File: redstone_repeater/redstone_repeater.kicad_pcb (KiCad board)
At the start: 2 copper layers, 40 x 40 mm, 46 parts, among them J1 1x4_Pogo, J2 1x4_Pogo, J3 1x4_Pogo, J4 1x4_Pogo, J5 1x4_Pogo, J6 1x4_Pogo, J7 1x4_Pogo, J8 1x4_Pogo, J9 2.54mm_ProgrammingPin, Q1 BC108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

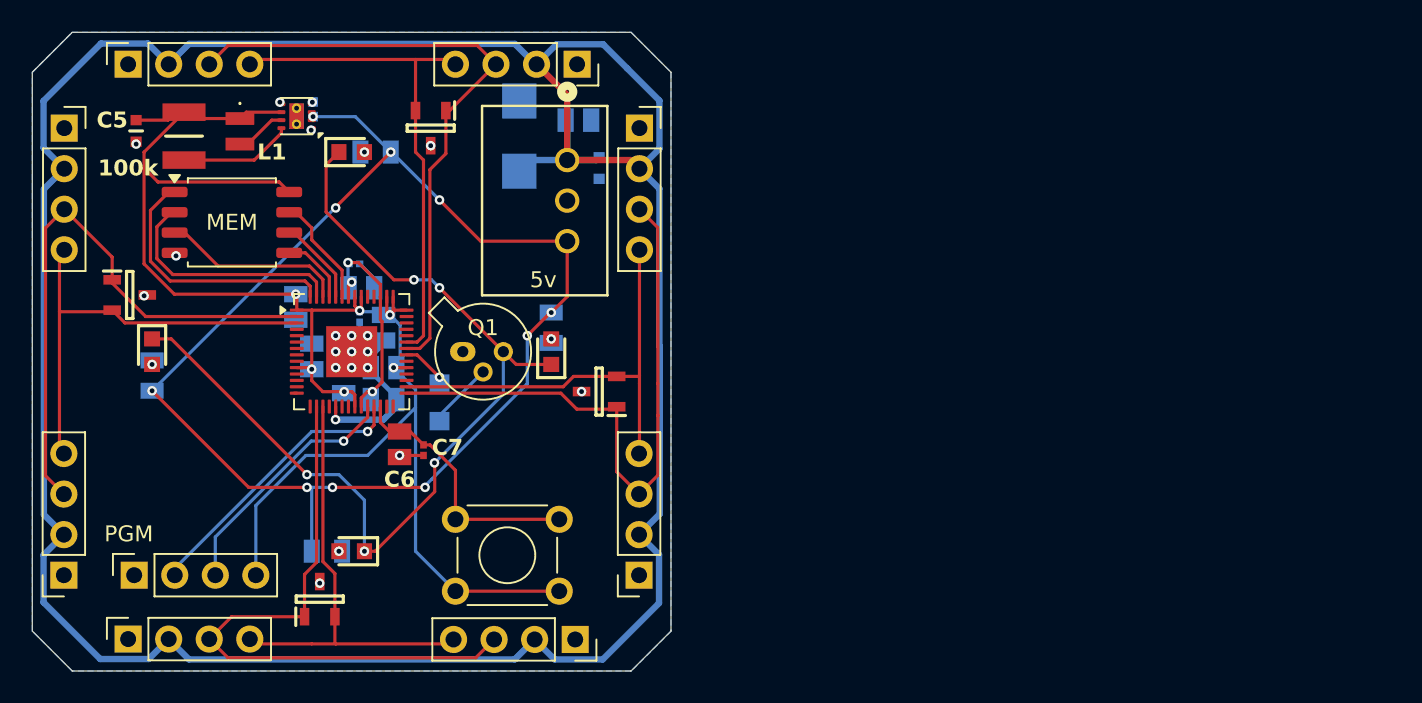
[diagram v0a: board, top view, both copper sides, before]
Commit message: add four individually controlled leds for repeater, small adjustments for redstone dust
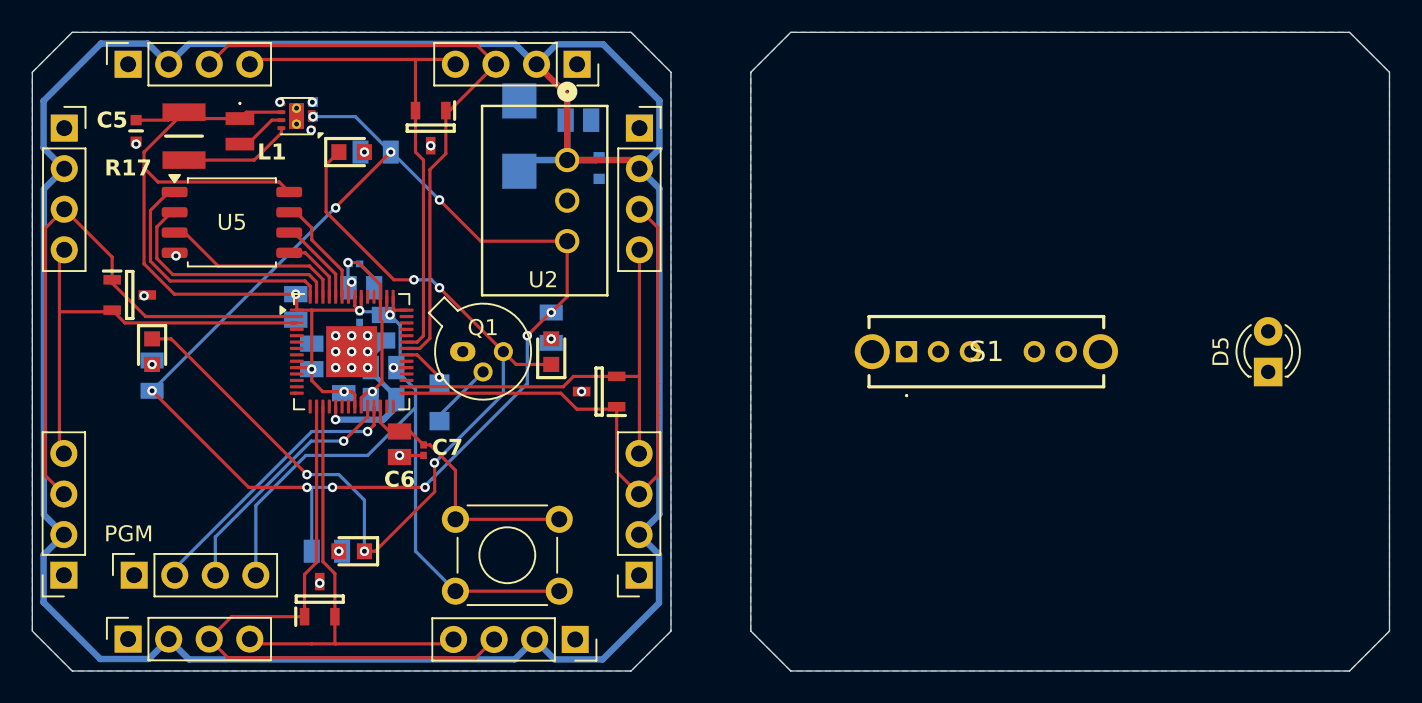
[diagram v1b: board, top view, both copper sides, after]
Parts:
- added D5: LED, LED_THT:LED_D3.0mm, F.Cu at (192.4, 56.3)
- added S1: SLW-1478144-5A-S-D, SamacSys_Parts:SLW14781445ASD, F.Cu at (169.8, 55.0)
- renumbered 200 to R1, 100k to R17, 1k to R5, 5v to U2, MEM to U5
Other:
- board size 40 x 40 mm -> 85 x 40 mm

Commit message: reorganize pcb layout for redstone repeater
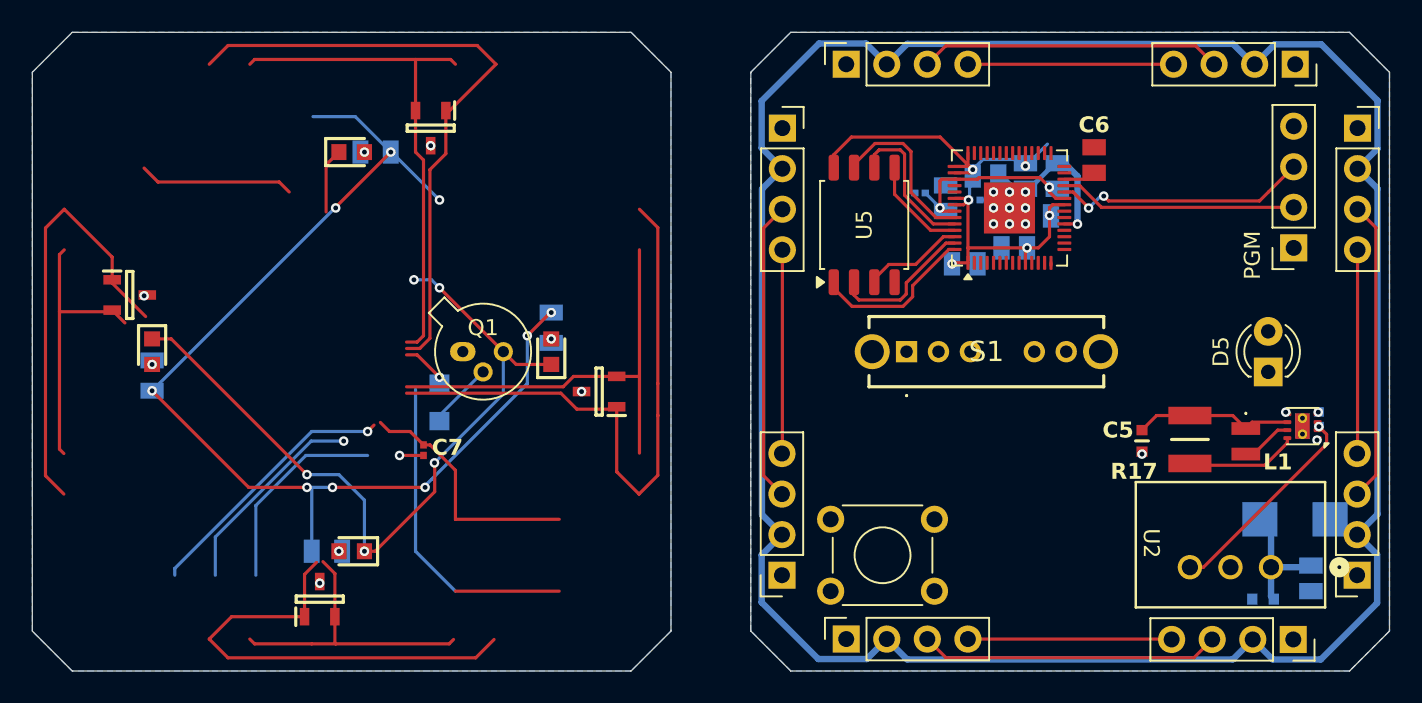
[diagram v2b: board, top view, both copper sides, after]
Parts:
- moved J9 75.5 mm to (194.0, 48.5), turned to 180 degrees
- moved C1 65.9 mm to (195.6, 59.2)
- moved C5 65.9 mm to (184.5, 60.6)
- moved L1 65.9 mm to (191.0, 60.6)
- moved U3 65.9 mm to (194.6, 59.7)
- moved R17 65.8 mm to (187.5, 60.5)
- moved D19 54.2 mm to (194.1, 65.5), turned to 0 degrees
- moved C3 54.1 mm to (195.1, 69.2), turned to -90 degrees
- moved U2 50.9 mm to (192.6, 68.5), turned to 180 degrees
- moved C4 49.6 mm to (192.1, 70.5), turned to 180 degrees
- moved C6 47.0 mm to (181.5, 43.0), turned to 90 degrees
- moved J1 45.0 mm to (166.0, 37.0)
- moved J2 45.0 mm to (194.1, 37.0)
- moved J3 45.0 mm to (198.0, 41.0)
- moved J4 45.0 mm to (198.0, 69.0)
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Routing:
- net /N_TX: track 39.7 -> 58.6 mm
- net /E_TX: track 38.5 -> 57.3 mm
- net /3.3V_LOCAL: track 105.0 -> 90.7 mm
- net Net-(J9-Pin_2): track 17.8 -> 31.5 mm
- net Net-(J9-Pin_3): track 15.7 -> 29.0 mm, vias 1 -> 3
- net /N_RX: track 31.9 -> 44.7 mm
- net /E_RX: track 27.6 -> 40.4 mm
- net VCC: track 173.7 -> 162.1 mm
- net /W_TX: track 37.1 -> 46.4 mm
- net /S_TX: track 38.8 -> 47.9 mm
- net Net-(D1-K): track 59.7 -> 52.5 mm
- net Net-(U1-QSPI_SS): track 17.0 -> 10.3 mm
- net Net-(U1-QSPI_SD1): track 15.0 -> 9.12 mm
- net Net-(U1-QSPI_SD2): track 12.2 -> 6.33 mm
- net Net-(U1-QSPI_SCLK): track 5.37 -> 9.39 mm
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
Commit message: finalize schematic and finish layout of pcb
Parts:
- added Q2: MMBT3904, Package_TO_SOT_SMD:SOT-23, F.Cu at (168.9, 62.5)
- added Q3: MMBT3904, Package_TO_SOT_SMD:SOT-23, F.Cu at (177.5, 62.5)
- added Q4: MMBT3904, Package_TO_SOT_SMD:SOT-23, F.Cu at (181.0, 62.5)
- added Q5: MMBT3904, Package_TO_SOT_SMD:SOT-23, F.Cu at (188.4, 55.9)
- added R10: 200, SamacSys_Parts:CRCW1210200RJNEAIF, F.Cu at (196.0, 56.5)
- added R6: 200, SamacSys_Parts:CRCW1210200RJNEAIF, B.Cu at (175.7, 58.5)
- added R7: 1k, SamacSys_Parts:ERJ-UP6D1001V, B.Cu at (180.5, 63.0)
- added R8: 200, SamacSys_Parts:CRCW1210200RJNEAIF, B.Cu at (179.2, 58.5)
- added R9: 1k, SamacSys_Parts:ERJ-UP6D1001V, F.Cu at (188.5, 51.3)
- Q1: value BC108 -> MMBT3904; footprint Package_TO_SOT_THT:TO-18-3 -> Package_TO_SOT_SMD:SOT-23
- R2, R4: value 200 -> 1k; footprint SamacSys_Parts:CRCW1210200RJNEAIF -> SamacSys_Parts:ERJ-UP6D1001V
- moved D4 57.4 mm to (179.7, 59.5), turned to 180 degrees
- moved R4 54.9 mm to (177.0, 63.0)
- moved C7 46.8 mm to (183.0, 43.8), turned to 90 degrees
- moved D18 46.3 mm to (196.5, 52.5), turned to 90 degrees
- moved D21 42.5 mm to (163.5, 54.0), turned to -90 degrees
- moved D3 42.0 mm to (176.2, 59.5)
- moved D20 41.5 mm to (174.5, 69.0)
- moved R3 39.8 mm to (172.2, 58.5), turned to -90 degrees
- moved D1 38.2 mm to (169.2, 59.5), turned to 180 degrees
- moved D17 37.6 mm to (177.5, 39.0), turned to 90 degrees
- moved R1 36.0 mm to (168.7, 58.5), turned to -90 degrees
- moved Q1 31.9 mm to (172.9, 62.5), turned to 180 degrees
- moved R2 26.7 mm to (172.5, 63.0), turned to 180 degrees
- moved R5 25.8 mm to (166.0, 62.0)
- moved D2 25.6 mm to (172.7, 59.5), turned to 180 degrees
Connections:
- D2 pad 1: Net-(D1-K) -> Net-(D2-K)
- D3 pad 1: Net-(D1-K) -> Net-(D3-K)
- D4 pad 1: Net-(D1-K) -> Net-(D4-K)
- D5 pad 1: unconnected-(D5-K-Pad1) -> Net-(D5-K)
- D5 pad 2: unconnected-(D5-A-Pad2) -> Net-(D5-A)
- Q1 pad 1: GND -> Net-(Q1-B)
- Q1 pad 2: Net-(Q1-B) -> GND
- Q1 pad 3: Net-(D1-K) -> Net-(D2-K)
- R2 pad 1: /5V_LOCAL -> Net-(Q1-B)
- R2 pad 2: Net-(D2-A) -> Net-(U1-GPIO7)
- R3 pad 2: Net-(D3-A) -> Net-(D2-A)
- R4 pad 1: /5V_LOCAL -> Net-(Q3-B)
- R4 pad 2: Net-(D4-A) -> Net-(U1-GPIO8)
- R5 pad 1: Net-(Q1-B) -> Net-(Q2-B)
- R5 pad 2: Net-(U1-GPIO23) -> Net-(U1-GPIO6)
- S1 pad 2: unconnected-(S1-NO_1-Pad2) -> Net-(S1-NO_1)
- S1 pad 4: unconnected-(S1-NO_2-Pad4) -> Net-(S1-NO_2)
- S1 pad 5: unconnected-(S1-NO_3-Pad5) -> Net-(S1-NO_3)
- U1 pad 11: unconnected-(U1-GPIO8-Pad11) -> Net-(U1-GPIO8)
- U1 pad 12: unconnected-(U1-GPIO9-Pad12) -> Net-(U1-GPIO9)
- U1 pad 13: unconnected-(U1-GPIO10-Pad13) -> /S_TX
- U1 pad 14: unconnected-(U1-GPIO11-Pad14) -> /S_RX
- U1 pad 15: unconnected-(U1-GPIO12-Pad15) -> Net-(U1-GPIO12)
- U1 pad 16: /S_TX -> /E_TX
- U1 pad 17: /S_RX -> /E_RX
- U1 pad 29: /E_TX -> unconnected-(U1-GPIO18-Pad29)
- U1 pad 30: /E_RX -> unconnected-(U1-GPIO19-Pad30)
- U1 pad 35: Net-(U1-GPIO23) -> unconnected-(U1-GPIO23-Pad35)
- U1 pad 36: /N_TX -> /N_RX
- U1 pad 37: /N_RX -> /N_TX
- U1 pad 5: unconnected-(U1-GPIO3-Pad5) -> Net-(S1-NO_1)
- U1 pad 6: unconnected-(U1-GPIO4-Pad6) -> Net-(S1-NO_2)
- U1 pad 7: unconnected-(U1-GPIO5-Pad7) -> Net-(S1-NO_3)
- U1 pad 8: unconnected-(U1-GPIO6-Pad8) -> Net-(U1-GPIO6)
- U1 pad 9: unconnected-(U1-GPIO7-Pad9) -> Net-(U1-GPIO7)
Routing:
- net /5V_LOCAL: track 82.9 -> 13.8 mm, vias 10 -> 1
- net Net-(D1-K): track 52.5 -> 0.00 mm, vias 5 -> 0
- net /3.3V_LOCAL: track 90.7 -> 48.1 mm
- net /N_TX: track 58.6 -> 18.9 mm
- net /E_TX: track 57.3 -> 18.8 mm
- net /N_RX: track 44.7 -> 12.9 mm
- net /S_TX: track 47.9 -> 18.8 mm
- net /W_TX: track 46.4 -> 18.8 mm
- net /E_RX: track 40.4 -> 12.8 mm
- net /S_RX: track 31.3 -> 12.9 mm
- net /W_RX: track 30.2 -> 12.8 mm
- net Net-(J9-Pin_2): track 31.5 -> 14.9 mm, vias 1 -> 0
- net Net-(SW1-B): track 17.5 -> 2.03 mm
- net Net-(J9-Pin_3): track 29.0 -> 16.1 mm, vias 3 -> 2
- net Net-(Q1-B): track 4.21 -> 0.00 mm
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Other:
- board size 85 x 40 mm -> 40 x 40 mm
- board text added: "${REFERENCE}"

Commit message: finish wiring layout
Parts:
- moved SW1 32.7 mm to (184.5, 40.0), turned to 0 degrees
- moved Q2 4.56 mm to (173.5, 62.5), turned to 90 degrees
- moved R5 4.12 mm to (170.0, 63.0)
- moved Q1 2.94 mm to (170.0, 62.5), turned to 90 degrees
- moved R2 1.00 mm to (173.5, 63.0), turned to 90 degrees
- moved Q4 0.50 mm to (180.5, 62.5)
- moved Q3 0.50 mm to (177.0, 62.5)
- moved R1 0.10 mm to (168.7, 58.5)
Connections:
- Q1 pad 3: Net-(D2-K) -> Net-(D1-K)
- Q2 pad 3: Net-(D1-K) -> Net-(D2-K)
- R2 pad 1: Net-(Q1-B) -> Net-(Q2-B)
- R5 pad 1: Net-(Q2-B) -> Net-(Q1-B)
- S1 pad 1: unconnected-(S1-NC-Pad1) -> Net-(S1-NC)
- U1 pad 34: unconnected-(U1-GPIO22-Pad34) -> /N_RX
- U1 pad 35: unconnected-(U1-GPIO23-Pad35) -> /N_TX
- U1 pad 36: /N_RX -> unconnected-(U1-GPIO24-Pad36)
- U1 pad 37: /N_TX -> unconnected-(U1-GPIO25-Pad37)
- U1 pad 4: unconnected-(U1-GPIO2-Pad4) -> Net-(S1-NC)
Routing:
- net /E_TX: track 18.8 -> 57.3 mm, vias 0 -> 1
- net /S_TX: track 18.8 -> 51.4 mm, vias 0 -> 2
- net /S_RX: track 12.9 -> 42.6 mm, vias 0 -> 2
- net /5V_LOCAL: track 13.8 -> 43.1 mm, vias 1 -> 5
- net /E_RX: track 12.8 -> 33.5 mm
- net /W_TX: track 18.8 -> 38.0 mm
- net /3.3V_LOCAL: track 48.1 -> 64.7 mm
- net Net-(U1-GPIO6): track 0.00 -> 16.5 mm, vias 0 -> 1
- net /W_RX: track 12.8 -> 27.8 mm
- net Net-(U1-GPIO7): track 0.00 -> 14.1 mm, vias 0 -> 1
- net Net-(U1-GPIO9): track 0.00 -> 13.6 mm, vias 0 -> 1
- net Net-(U1-GPIO8): track 0.00 -> 13.1 mm, vias 0 -> 1
- net Net-(SW1-B): track 2.03 -> 11.8 mm
- net Net-(U1-GPIO12): track 0.00 -> 9.50 mm
- net /N_TX: track 18.9 -> 28.2 mm
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
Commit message: run drc, fix silkscreen, fix drc errors
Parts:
- moved D19 3.78 mm to (190.3, 65.5), turned to 180 degrees
- moved L1 0.61 mm to (191.0, 60.0)
- moved J7 0.08 mm to (162.1, 41.0)
- moved J8 0.05 mm to (162.0, 69.0)
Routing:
- net /3.3V_LOCAL: track 64.7 -> 82.6 mm, vias 6 -> 7
- net VCC: track 162.1 -> 165.7 mm
- net GND: vias 24 -> 25
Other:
- board text removed: "${REFERENCE}"

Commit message: generate gerber files for all blocks
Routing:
- net GND: track 15.8 -> 17.7 mm
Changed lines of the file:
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@@
 			(outputformat 1)
 			(mirror no)
-			(drillshape 1)
+			(drillshape 0)
 			(scaleselection 1)
 			(outputdirectory "")
@@
 	)
 	(segment
+		(start 171.61 44)
+		(end 170.5 44)
+		(width 0.4)
+		(layer "B.Cu")
+		(net 2)
+	)
+	(segment
 		(start 177.447 44.8)
 		(end 177.2 44.8)
@@
 		(layer "B.Cu")
 		(net 2)
+	)
+	(segment
+		(start 172.2 44.59)
+		(end 171.61 44)
+		(width 0.4)
+		(layer "B.Cu")
+		(net 2)
